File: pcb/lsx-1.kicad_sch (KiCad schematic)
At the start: 7 parts, among them J1 RJ45, J2 USART-USB, J3 ISP

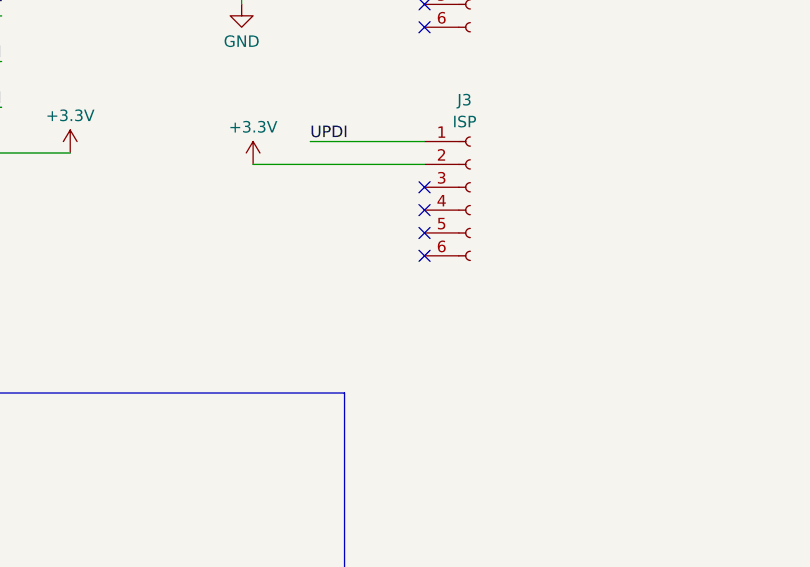
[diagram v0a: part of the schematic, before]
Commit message: Corrects the GND on the ISP
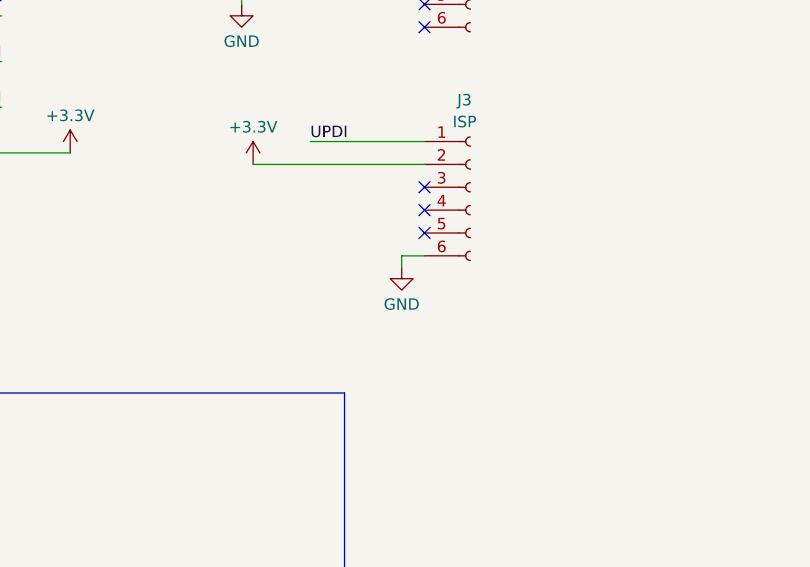
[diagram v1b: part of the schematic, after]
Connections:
- net GND: now also J3.6 (Pin_6)
- no-connect marks 7 -> 6
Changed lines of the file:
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@@
 	(title_block
 		(title "Leawood Sensor Adapter LSX-1")
-		(date "2024-03-27")
-		(rev "1.0")
+		(date "2024-05-12")
+		(rev "1.1")
 	)
 	(junction
@@
 	)
 	(no_connect
-		(at 156.21 85.09)
-	)
-	(no_connect
 		(at 156.21 59.69)
 	)
@@
 	(wire
 		(pts
+			(xy 153.67 85.09) (xy 153.67 86.36)
+		)
+		(stroke
+			(width 0)
+			(type default)
+		)
+	)
+	(wire
+		(pts
 			(xy 135.89 54.61) (xy 135.89 57.15)
 		)
@@
 	(wire
 		(pts
+			(xy 156.21 85.09) (xy 153.67 85.09)
+		)
+		(stroke
+			(width 0)
+			(type default)
+		)
+	)
+	(wire
+		(pts
 			(xy 143.51 52.07) (xy 156.21 52.07)
 		)
@@
 					(unit 1)
 				)
+			)
+		)
+	)
+	(symbol
+		(lib_id "power:GND")
+		(at 153.67 86.36 0)
+		(unit 1)
+		(exclude_from_sim no)
+		(in_bom yes)
+		(on_board yes)
+		(dnp no)
+		(fields_autoplaced yes)
+		(property "Reference" "#PWR05"
+			(at 153.67 92.71 0)
+			(effects
+				(font
+					(size 1.27 1.27)
+				)
+				(hide yes)
+			)
+		)
+		(property "Value" "GND"
+			(at 153.67 90.4931 0)
+			(effects
+				(font
+					(size 1.27 1.27)
+				)
+			)
+		)
+		(property "Footprint" ""
+			(at 153.67 86.36 0)
+			(effects
+				(font
+					(size 1.27 1.27)
+				)
+				(hide yes)
+			)
+		)
+		(property "Datasheet" ""
+			(at 153.67 86.36 0)
+			(effects
+				(font
+					(size 1.27 1.27)
+				)
+				(hide yes)
+			)
+		)
+		(property "Description" "Power symbol creates a global label with name \"GND\" , ground"
+			(at 153.67 86.36 0)
+			(effects
+				(font
+					(size 1.27 1.27)
+				)
+				(hide yes)
+			)
+		)
+		(pin "1"
+		)
+		(instances
+			(project "lsx-1"
+				(path "/d65bd730-f94a-4250-99f3-f4d7cbd238f8"
+					(reference "#PWR05")
+					(unit 1)
+				)

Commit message: Update
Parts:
- added H1, H2, H3, H4: MountingHole, MountingHole:MountingHole_2.7mm_M2.5, symbol Mechanical:MountingHole
- J2: footprint Connector_PinSocket_2.54mm:PinSocket_1x06_P2.54mm_Vertical -> Connector_PinHeader_2.54mm:PinHeader_1x06_P2.54mm_Horizontal
- J3: footprint Connector_IDC:IDC-Header_2x03_P2.54mm_Vertical -> Connector_PinHeader_2.54mm:PinHeader_2x03_P2.54mm_Horizontal
